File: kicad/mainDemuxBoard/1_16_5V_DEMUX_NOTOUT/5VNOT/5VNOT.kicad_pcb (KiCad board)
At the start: 4 copper layers, 2 parts, among them Q1025 PMOS, Q1026 NMOS

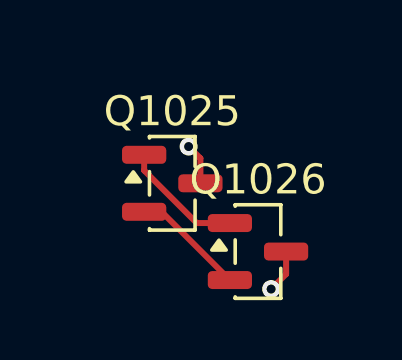
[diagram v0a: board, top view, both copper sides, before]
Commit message: update main board schematic
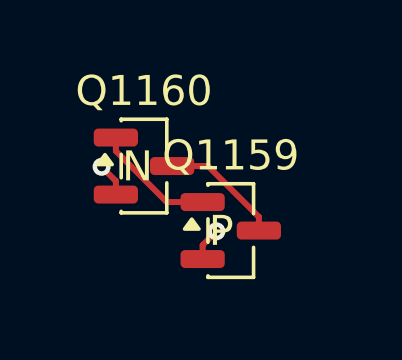
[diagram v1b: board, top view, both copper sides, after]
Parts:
- removed Q1025: PMOS, Package_TO_SOT_SMD:SOT-23
- removed Q1026: NMOS, Package_TO_SOT_SMD:SOT-23
- added Q1159: Q_PMOS_GSD, easyeda2kicad:SOT-23-P, F.Cu at (99.0, 66.5)
- added Q1160: Q_NMOS_GSD, easyeda2kicad:SOT-23-N, F.Cu at (96.1, 64.4)
